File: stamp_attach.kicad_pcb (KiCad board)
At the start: 2 copper layers, 14.1 x 11 mm, 10 parts, among them J1 TOP

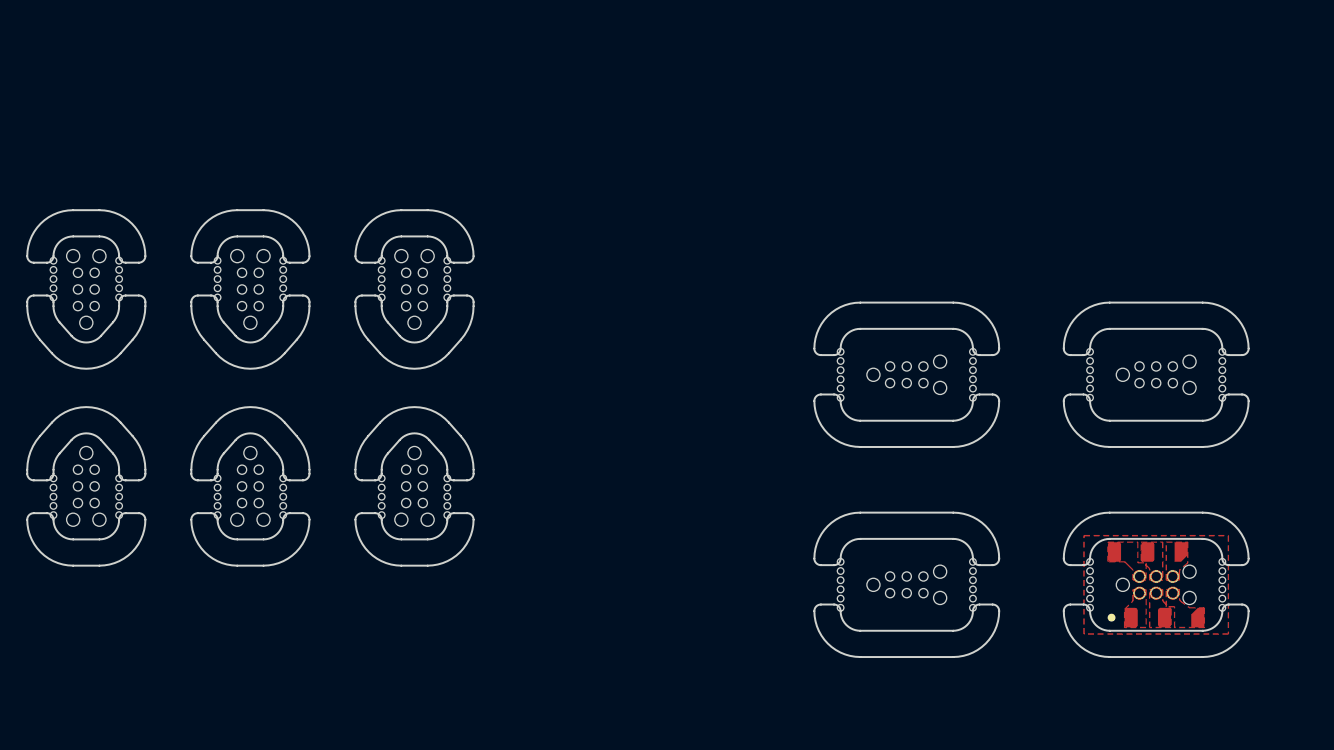
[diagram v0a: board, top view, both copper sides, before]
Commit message: updated footprint arrangement and quantity
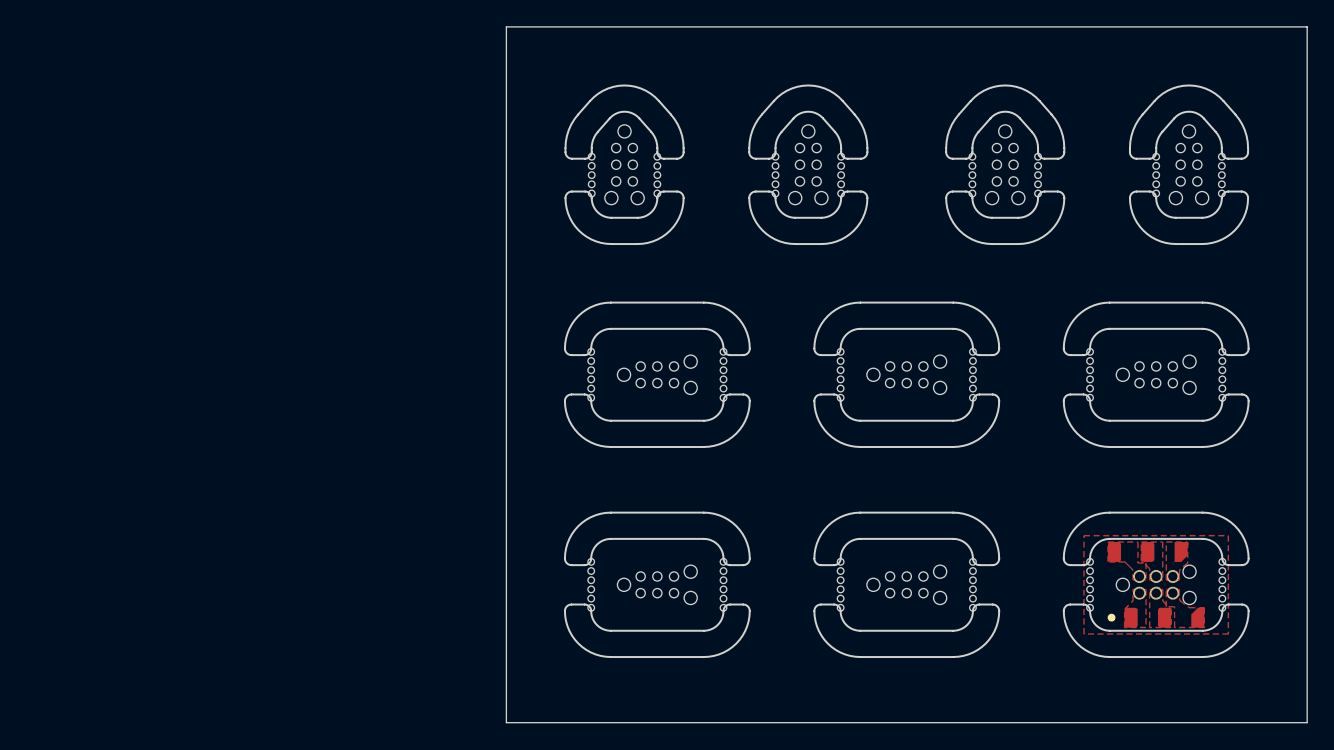
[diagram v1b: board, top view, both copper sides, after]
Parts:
- removed the REF** at (111.0, 104.5)
- removed the REF** at (111.0, 119.5)
- added REF**: SA_mid_layer, Stamp_Attach:SA_mid_layer, F.Cu at (129.5, 127.0)
- added REF**: SA_mid_layer, Stamp_Attach:SA_mid_layer, F.Cu at (129.5, 111.0)
- moved REF** 84.5 mm to (170.0, 95.0), turned to -90 degrees
- moved REF** 58.3 mm to (156.0, 95.0), turned to -90 degrees
- moved REF** 49.1 mm to (141.0, 95.0)
- moved REF** 47.8 mm to (127.0, 95.0)
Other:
- board size 14.1 x 11 mm -> 61 x 53 mm

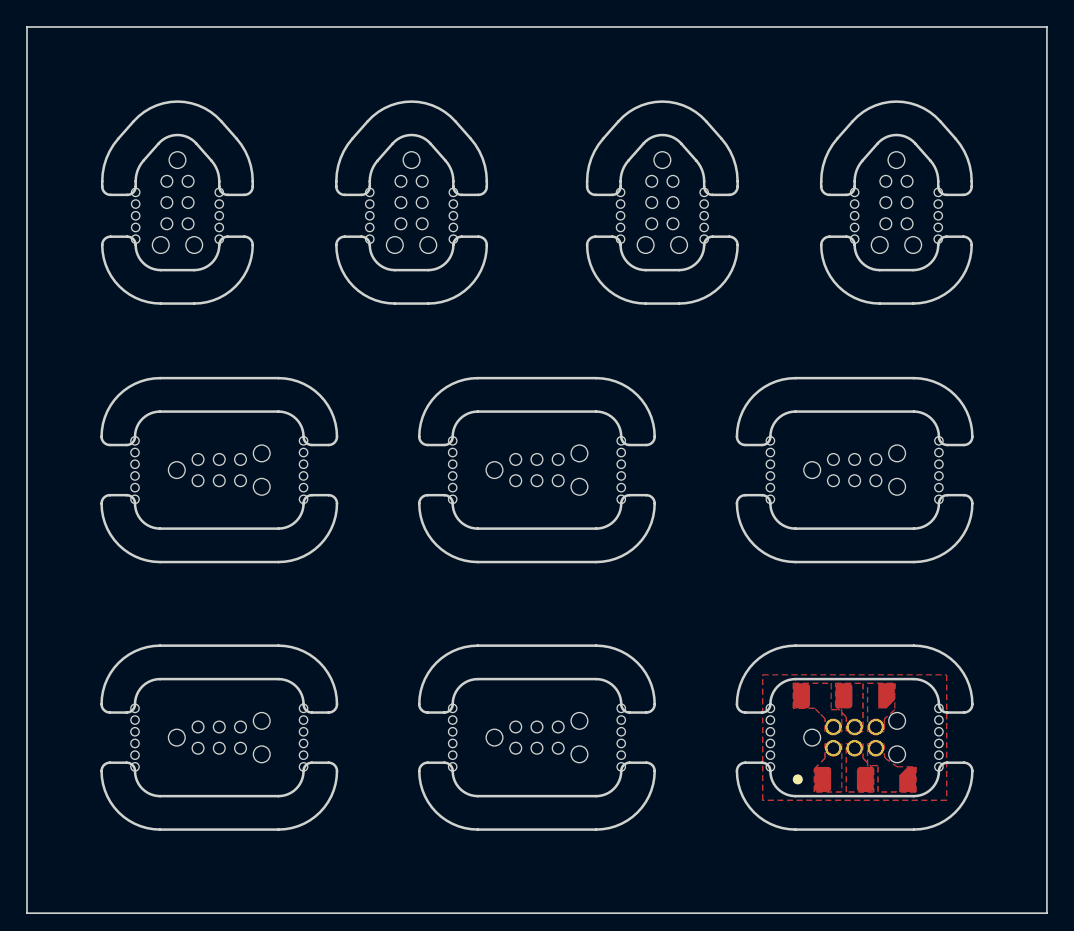
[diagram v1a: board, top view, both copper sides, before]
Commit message: updated footprints with oval pads; added solder points for bottom PCB
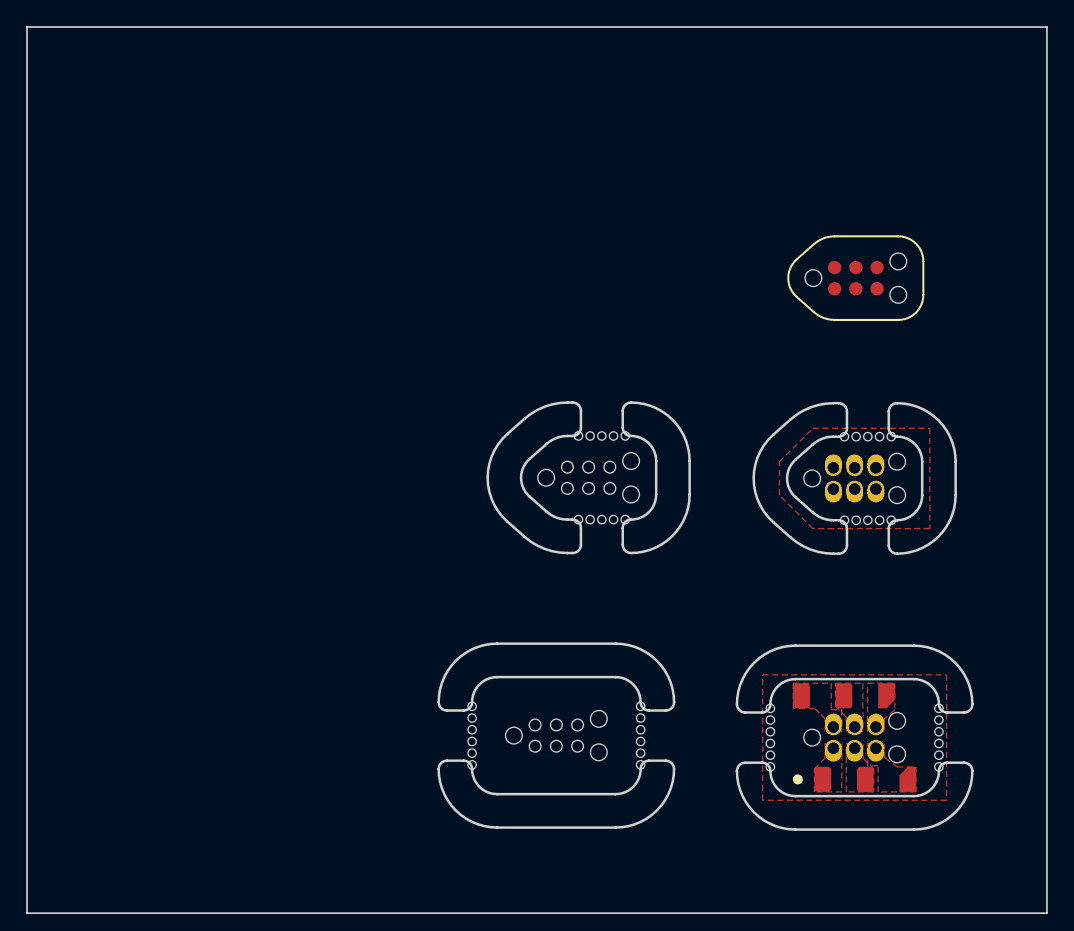
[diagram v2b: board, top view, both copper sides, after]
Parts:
- removed the REF** at (129.5, 127.0)
- removed the REF** at (127.0, 95.0)
- removed the REF** at (167.5, 111.0)
- removed the REF** at (141.0, 95.0)
- removed the REF** at (170.0, 95.0)
- removed the REF** at (156.0, 95.0)
- removed the REF** at (148.5, 111.0)
- removed the REF** at (129.5, 111.0)
- removed the REF** at (148.5, 127.0)
- added REF**: SA_layer_C, Stamp_Attach:SA_layer_C, F.Cu at (151.6, 111.5)
- added REF**: Stamp-Attach_SA2030-IDC-NL_2x03_P1.27mm_Vertical, Stamp_Attach:Stamp-Attach_SA2030-IDC-NL_2x03_P1.27mm_Vertical, F.Cu at (167.6, 99.5)
- added REF**: SA_layer_B, Stamp_Attach:SA_layer_B, F.Cu at (149.7, 126.9)
- added REF**: SA_layer_D, Stamp_Attach:SA_layer_D, F.Cu at (167.5, 111.5)
- J1: value TOP -> SA_layer_A; footprint Stamp_Attach:SA_top_layer -> Stamp_Attach:SA_layer_A

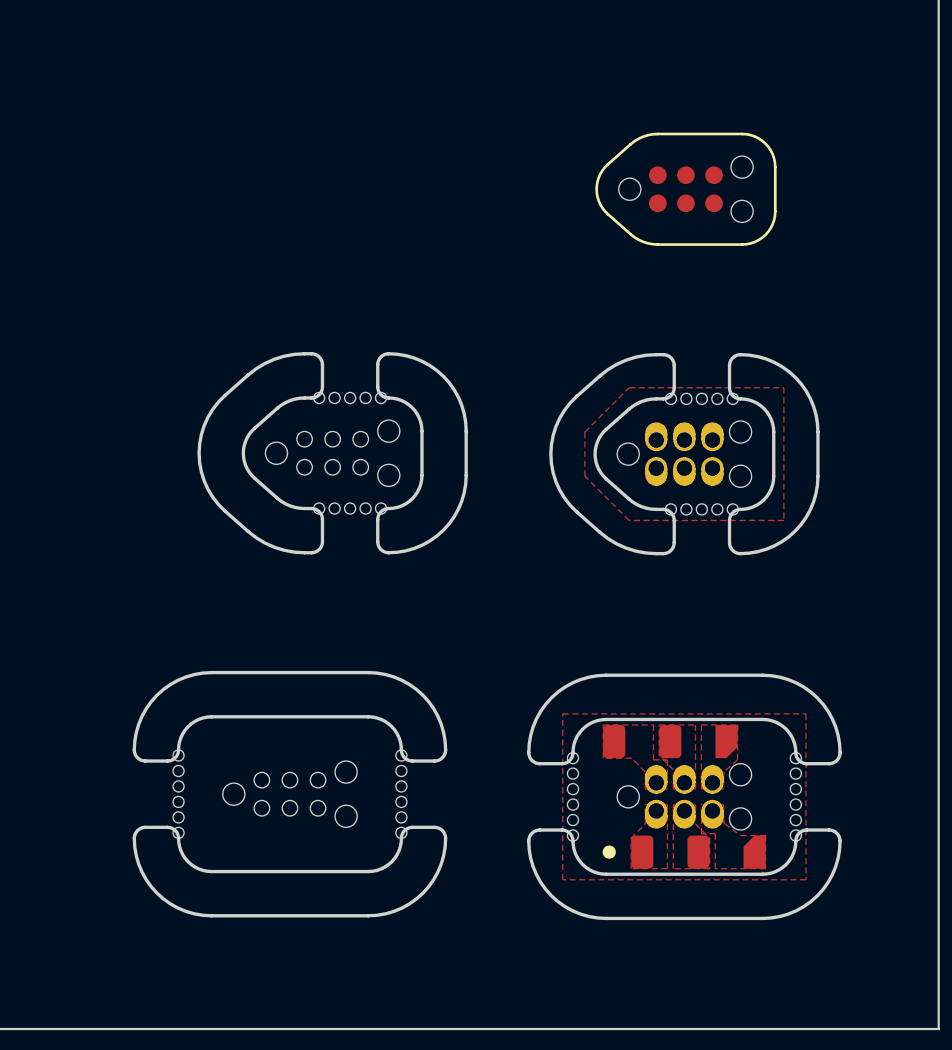
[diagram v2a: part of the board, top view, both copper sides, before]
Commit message: updated footprints; changed pads to be 0.25mm spacing and clearance; made the mounting holes PTH with custom pad
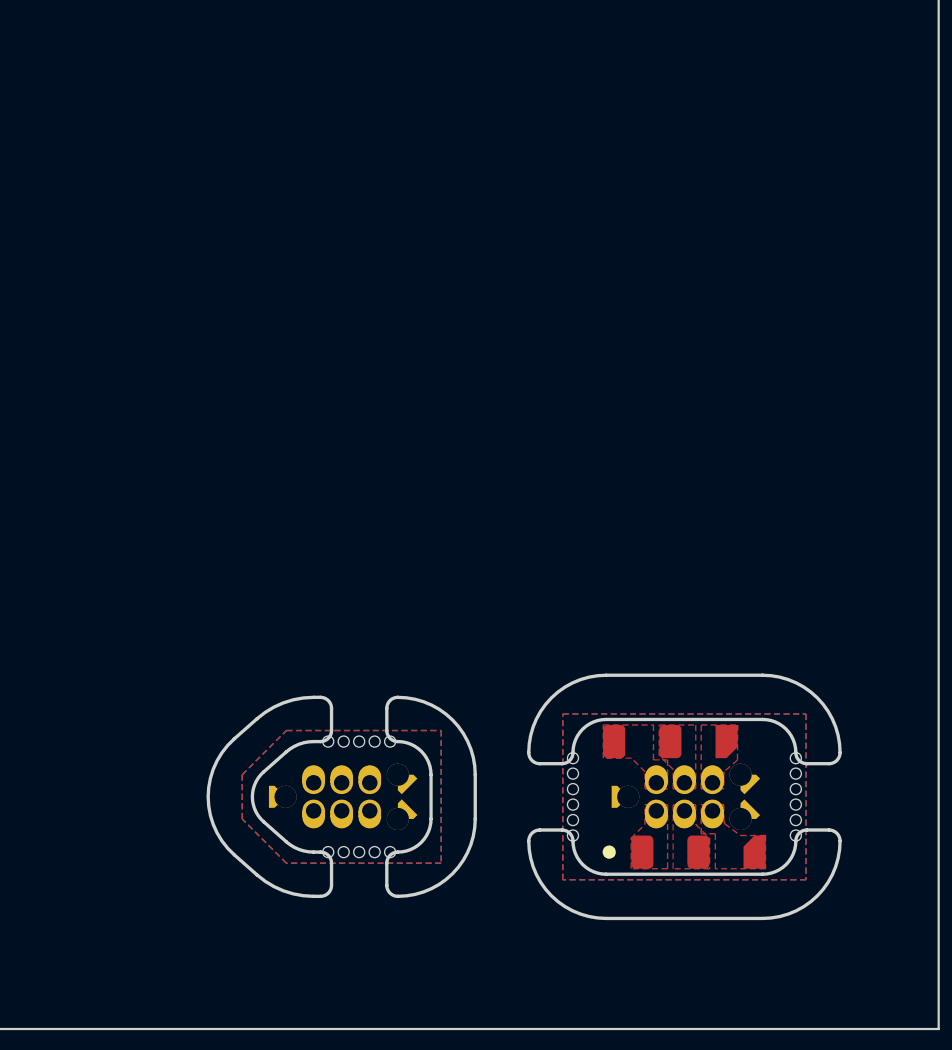
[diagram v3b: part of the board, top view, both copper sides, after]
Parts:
- removed REF**: SA_layer_C, Stamp_Attach:SA_layer_C
- removed REF**: Stamp-Attach_SA2030-IDC-NL_2x03_P1.27mm_Vertical, Stamp_Attach:Stamp-Attach_SA2030-IDC-NL_2x03_P1.27mm_Vertical
- removed REF**: SA_layer_B, Stamp_Attach:SA_layer_B
- removed REF**: SA_layer_D, Stamp_Attach:SA_layer_D
- added J2: SA_layer_D, Stamp_Attach:SA_layer_D, F.Cu at (152.0, 127.0)
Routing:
- added copper zone on B.Cu, net unconnected-(J1-PadMP)
- added copper zone on F.Cu, net unconnected-(J1-PadMP)
- added copper zone on B.Cu, net unconnected-(J2-PadMP)
- added copper zone on F.Cu, net unconnected-(J2-PadMP)
- removed copper zone on F.Cu, net (none)

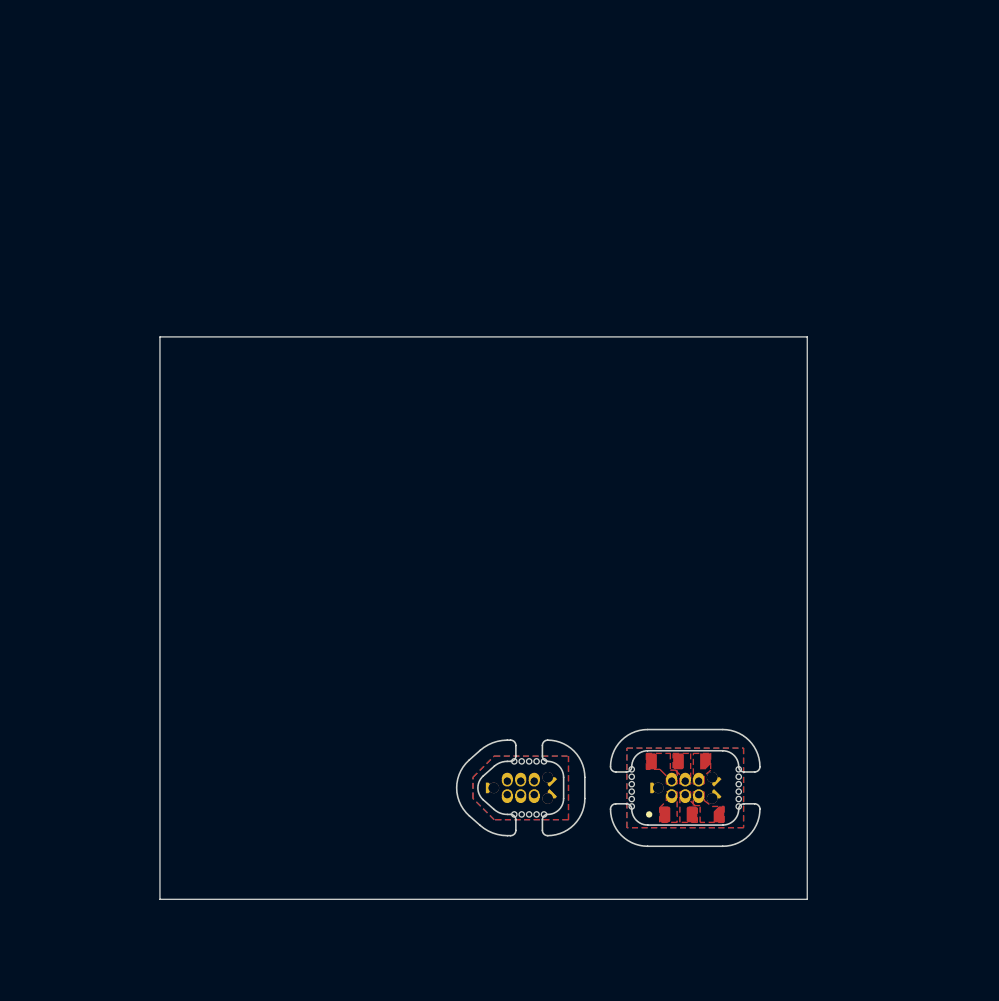
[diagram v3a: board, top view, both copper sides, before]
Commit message: Updated panel with graphics area and mousebites
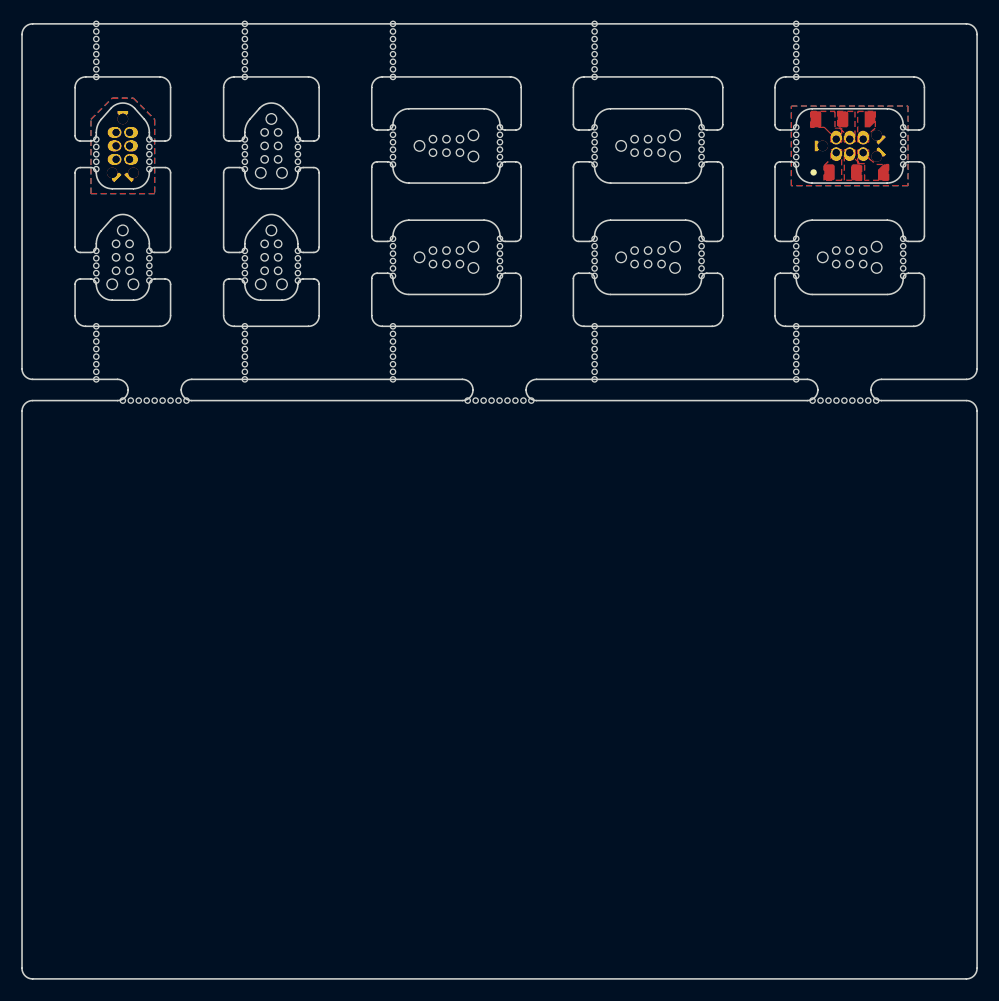
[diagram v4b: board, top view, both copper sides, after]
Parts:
- added REF**: Tab_Mousebites_5mm_2mm, Stamp_Attach:Tab_Mousebites_5mm_2mm, F.Cu at (182.5, 89.5)
- added REF**: SA_layer_B, Stamp_Attach:SA_layer_B, F.Cu at (145.0, 66.5)
- added REF**: SA_layer_B, Stamp_Attach:SA_layer_B, F.Cu at (164.0, 77.0)
- added REF**: Cut_Mousebites_5mm, Stamp_Attach:Cut_Mousebites_5mm, F.Cu at (112.0, 57.5)
- added REF**: Cut_Mousebites_5mm, Stamp_Attach:Cut_Mousebites_5mm, F.Cu at (178.0, 86.0)
- added REF**: SA_layer_B, Stamp_Attach:SA_layer_B, F.Cu at (164.0, 66.5)
- added REF**: Tab_Mousebites_5mm_2mm, Stamp_Attach:Tab_Mousebites_5mm_2mm, F.Cu at (150.0, 89.5)
- added REF**: SA_layer_B, Stamp_Attach:SA_layer_B, F.Cu at (183.0, 77.0)
- added REF**: Cut_Mousebites_5mm, Stamp_Attach:Cut_Mousebites_5mm, F.Cu at (159.0, 57.5)
- added REF**: Cut_Mousebites_5mm, Stamp_Attach:Cut_Mousebites_5mm, F.Cu at (112.0, 86.0)
- added REF**: Cut_Mousebites_5mm, Stamp_Attach:Cut_Mousebites_5mm, F.Cu at (126.0, 86.0)
- added REF**: Tab_Mousebites_5mm_2mm, Stamp_Attach:Tab_Mousebites_5mm_2mm, F.Cu at (117.5, 89.5)
- added REF**: SA_layer_C, Stamp_Attach:SA_layer_C, F.Cu at (114.5, 77.0)
- added REF**: SA_layer_C, Stamp_Attach:SA_layer_C, F.Cu at (128.5, 66.5)
- added REF**: Cut_Mousebites_5mm, Stamp_Attach:Cut_Mousebites_5mm, F.Cu at (126.0, 57.5)
- added REF**: Cut_Mousebites_5mm, Stamp_Attach:Cut_Mousebites_5mm, F.Cu at (178.0, 57.5)
- added REF**: Cut_Mousebites_5mm, Stamp_Attach:Cut_Mousebites_5mm, F.Cu at (140.0, 86.0)
- added REF**: Cut_Mousebites_5mm, Stamp_Attach:Cut_Mousebites_5mm, F.Cu at (140.0, 57.5)
- added REF**: Cut_Mousebites_5mm, Stamp_Attach:Cut_Mousebites_5mm, F.Cu at (159.0, 86.0)
- added REF**: SA_layer_B, Stamp_Attach:SA_layer_B, F.Cu at (145.0, 77.0)
- added REF**: SA_layer_C, Stamp_Attach:SA_layer_C, F.Cu at (128.5, 77.0)
- moved J2 71.2 mm to (114.5, 66.5), turned to -90 degrees
- moved J1 62.5 mm to (183.0, 66.5)
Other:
- board size 61 x 53 mm -> 90 x 90 mm

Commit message: silk art
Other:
- board text added: "A"
- board text added: "B"
- board text added: "C"
- board text added: "D"

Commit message: OSH buns
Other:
- board size 90 x 90 mm -> 90 x 74 mm
